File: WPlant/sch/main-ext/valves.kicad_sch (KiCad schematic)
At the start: 23 parts, among them J6 Conn_01x08_Pin, Q1 FDS9926A, Q2 FDS9926A, Q3 FDS9926A, Q4 FDS9926A, U7 74HC594

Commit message: Route of MainInt PCB done
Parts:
- J6: footprint easyeda2kicad:CONN-TH_8P-P2.50_XAD-8A -> locals:CONN-TH_8P-P2.50_XAD-8AS
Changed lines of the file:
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@@
 			)
 		)
-		(property "Footprint" "easyeda2kicad:CONN-TH_8P-P2.50_XAD-8A"
+		(property "Footprint" "locals:CONN-TH_8P-P2.50_XAD-8AS"
 			(at 212.09 93.98 0)
 			(effects

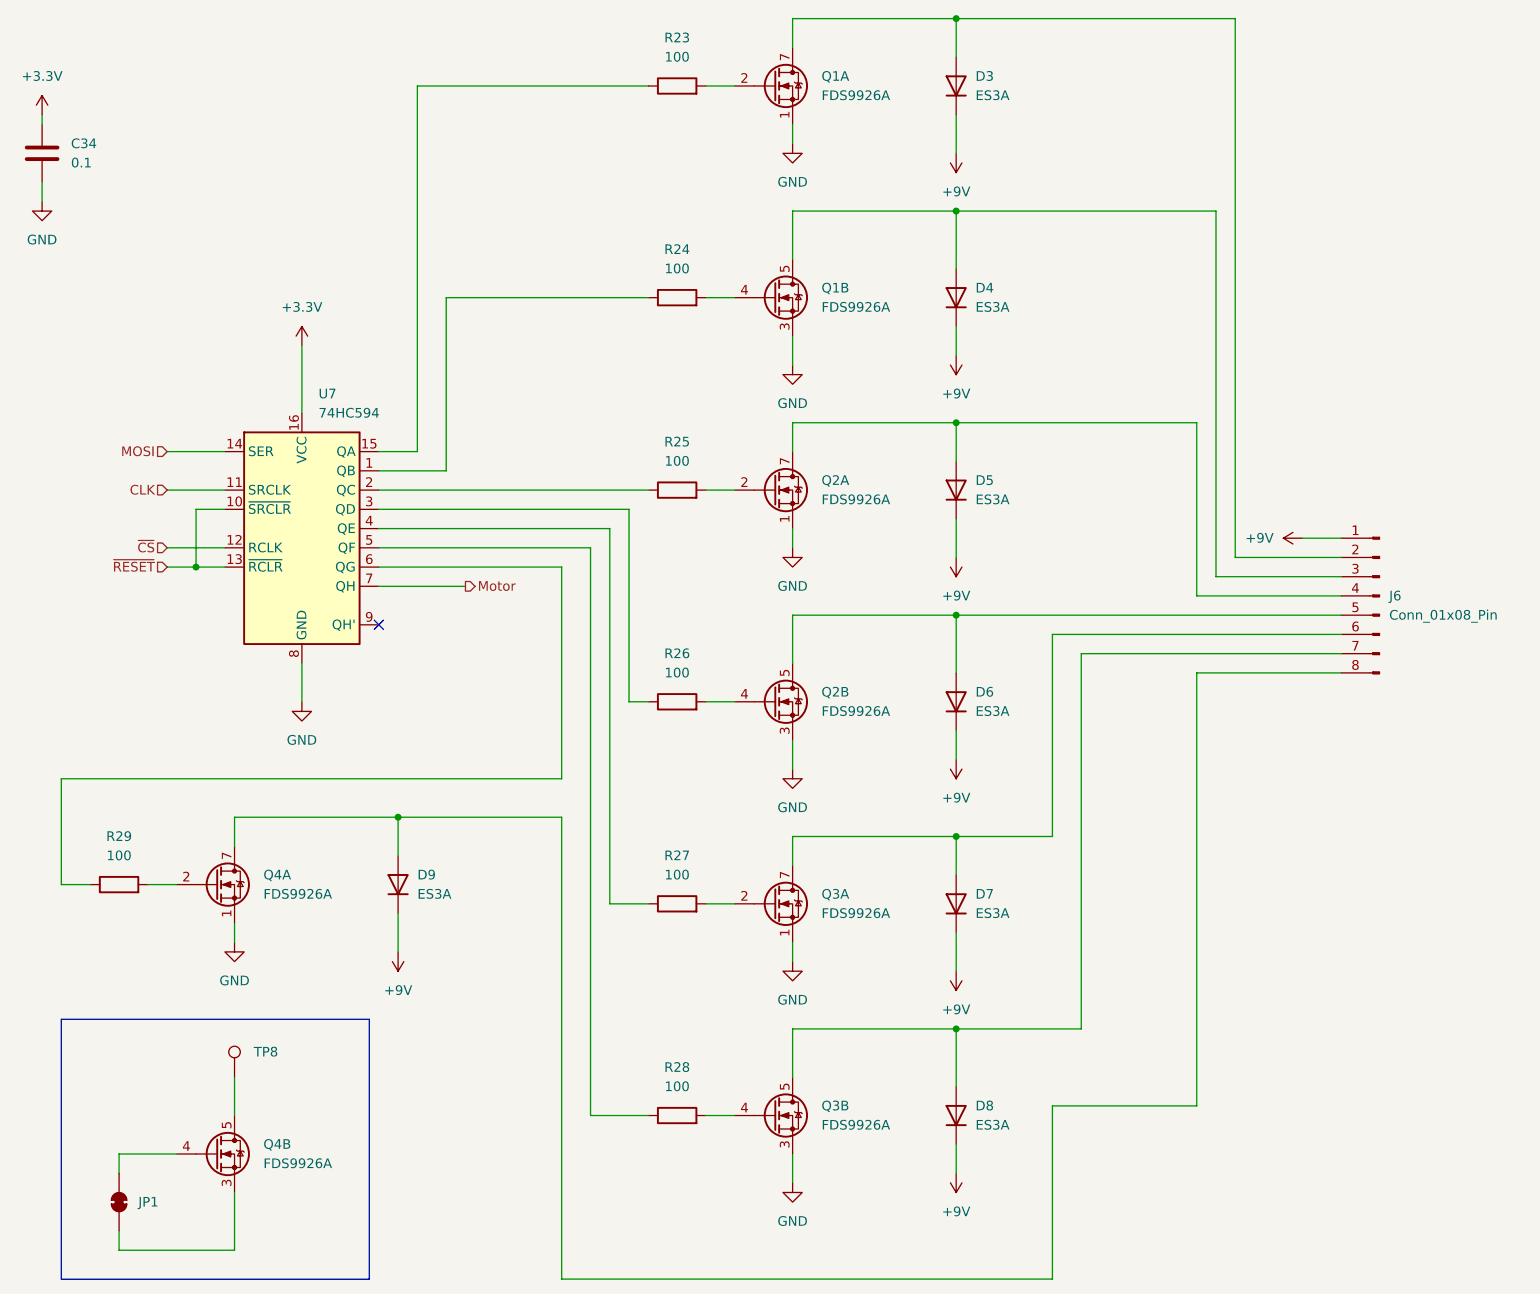
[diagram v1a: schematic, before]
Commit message: Route of MainExt PCB done
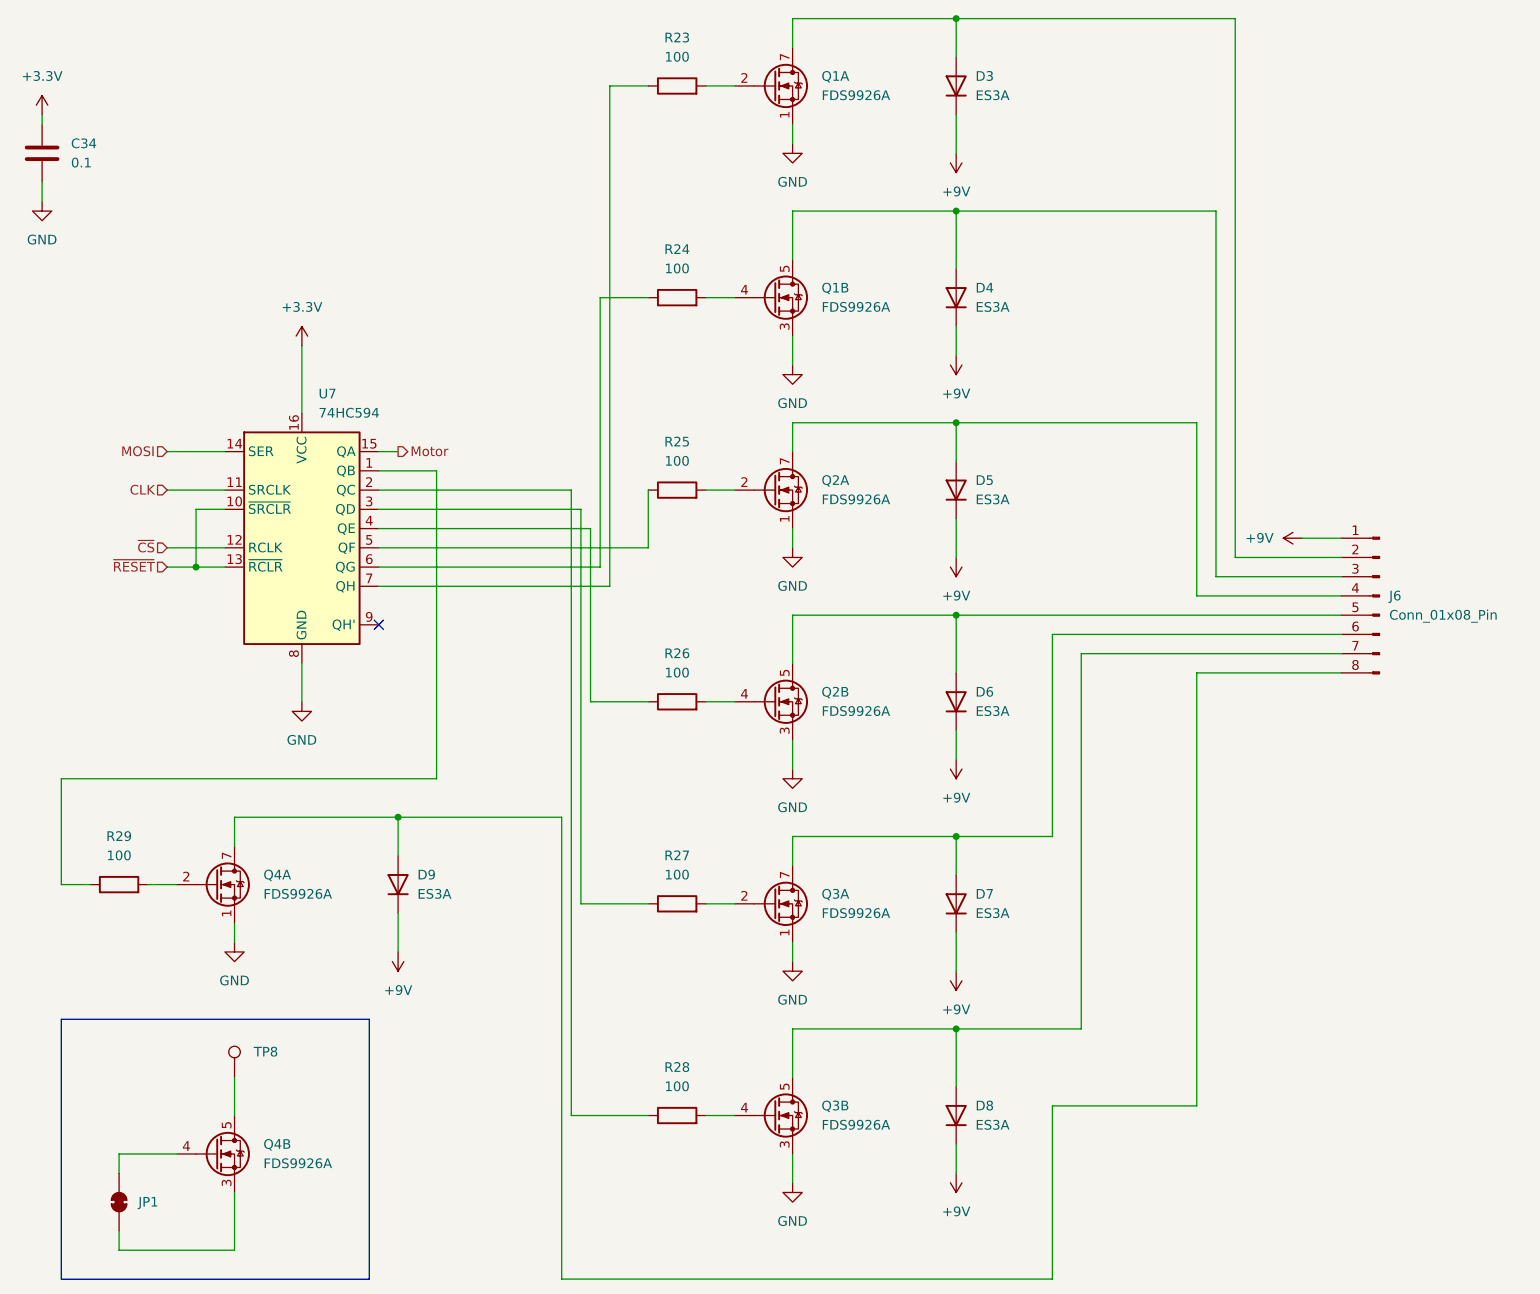
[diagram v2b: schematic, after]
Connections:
- net Motor: now also U7.15 (QA); no longer U7.7 (QH)
- net at R23.1: now also U7.7 (QH); no longer U7.15 (QA)
- net at R29.1: now also U7.1 (QB); no longer U7.6 (QG)
- net at R25.1: now also U7.5 (QF); no longer U7.2 (QC)
- net at R27.1: now also U7.3 (QD); no longer U7.4 (QE)
- net at R24.1: now also U7.6 (QG); no longer U7.1 (QB)
- net at R26.1: now also U7.4 (QE); no longer U7.3 (QD)
- net at R28.1: now also U7.2 (QC); no longer U7.5 (QF)
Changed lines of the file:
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@@
+	(wire
+		(pts
+			(xy 80.01 92.71) (xy 110.49 92.71)
+		)
+		(stroke
+			(width 0)
+			(type default)
+		)
+	)
 	(wire
 		(pts
@@
 	(wire
 		(pts
+			(xy 110.49 26.67) (xy 110.49 92.71)
+		)
+		(stroke
+			(width 0)
+			(type default)
+		)
+	)
+	(wire
+		(pts
+			(xy 106.68 82.55) (xy 106.68 134.62)
+		)
+		(stroke
+			(width 0)
+			(type default)
+		)
+	)
+	(wire
+		(pts
 			(xy 59.69 82.55) (xy 55.88 82.55)
 		)
@@
 	(wire
 		(pts
-			(xy 85.09 26.67) (xy 115.57 26.67)
-		)
-		(stroke
-			(width 0)
-			(type default)
-		)
-	)
-	(wire
-		(pts
 			(xy 156.21 96.52) (xy 207.01 96.52)
 		)
@@
 	(wire
 		(pts
-			(xy 80.01 80.01) (xy 115.57 80.01)
+			(xy 80.01 85.09) (xy 107.95 85.09)
 		)
 		(stroke
@@
 	(wire
 		(pts
-			(xy 113.03 82.55) (xy 113.03 107.95)
-		)
-		(stroke
-			(width 0)
-			(type default)
-		)
-	)
-	(wire
-		(pts
 			(xy 69.85 60.96) (xy 69.85 69.85)
 		)
@@
 	(wire
 		(pts
+			(xy 115.57 87.63) (xy 115.57 80.01)
+		)
+		(stroke
+			(width 0)
+			(type default)
+		)
+	)
+	(wire
+		(pts
+			(xy 105.41 80.01) (xy 105.41 162.56)
+		)
+		(stroke
+			(width 0)
+			(type default)
+		)
+	)
+	(wire
+		(pts
 			(xy 45.72 177.8) (xy 45.72 180.34)
 		)
@@
 	(wire
 		(pts
-			(xy 113.03 107.95) (xy 115.57 107.95)
+			(xy 107.95 107.95) (xy 115.57 107.95)
 		)
 		(stroke
@@
 	(wire
 		(pts
+			(xy 110.49 26.67) (xy 115.57 26.67)
+		)
+		(stroke
+			(width 0)
+			(type default)
+		)
+	)
+	(wire
+		(pts
 			(xy 60.96 162.56) (xy 60.96 157.48)
 		)
@@
 	(wire
 		(pts
-			(xy 104.14 118.11) (xy 38.1 118.11)
-		)
-		(stroke
-			(width 0)
-			(type default)
-		)
-	)
-	(wire
-		(pts
-			(xy 80.01 82.55) (xy 113.03 82.55)
+			(xy 87.63 118.11) (xy 38.1 118.11)
 		)
 		(stroke
@@
 	(wire
 		(pts
+			(xy 107.95 85.09) (xy 107.95 107.95)
+		)
+		(stroke
+			(width 0)
+			(type default)
+		)
+	)
+	(wire
+		(pts
 			(xy 134.62 125.73) (xy 156.21 125.73)
 		)
@@
 	(wire
 		(pts
+			(xy 87.63 77.47) (xy 80.01 77.47)
+		)
+		(stroke
+			(width 0)
+			(type default)
+		)
+	)
+	(wire
+		(pts
 			(xy 52.07 80.01) (xy 59.69 80.01)
 		)
@@
 	(wire
 		(pts
-			(xy 104.14 90.17) (xy 104.14 118.11)
-		)
-		(stroke
-			(width 0)
-			(type default)
-		)
-	)
-	(wire
-		(pts
 			(xy 52.07 87.63) (xy 59.69 87.63)
 		)
@@
 	(wire
 		(pts
-			(xy 80.01 92.71) (xy 91.44 92.71)
-		)
-		(stroke
-			(width 0)
-			(type default)
-		)
-	)
-	(wire
-		(pts
 			(xy 134.62 71.12) (xy 156.21 71.12)
 		)
@@
 	(wire
 		(pts
-			(xy 110.49 134.62) (xy 115.57 134.62)
+			(xy 80.01 87.63) (xy 115.57 87.63)
+		)
+		(stroke
+			(width 0)
+			(type default)
+		)
+	)
+	(wire
+		(pts
+			(xy 106.68 134.62) (xy 115.57 134.62)
 		)
 		(stroke
@@
 	(wire
 		(pts
-			(xy 80.01 85.09) (xy 110.49 85.09)
-		)
-		(stroke
-			(width 0)
-			(type default)
-		)
-	)
-	(wire
-		(pts
-			(xy 80.01 77.47) (xy 88.9 77.47)
-		)
-		(stroke
-			(width 0)
-			(type default)
-		)
-	)
-	(wire
-		(pts
 			(xy 172.72 101.6) (xy 207.01 101.6)
 		)
@@
 	(wire
 		(pts
-			(xy 88.9 77.47) (xy 88.9 54.61)
-		)
-		(stroke
-			(width 0)
-			(type default)
-		)
-	)
-	(wire
-		(pts
 			(xy 201.93 86.36) (xy 207.01 86.36)
 		)
@@
 	(wire
 		(pts
-			(xy 80.01 90.17) (xy 104.14 90.17)
-		)
-		(stroke
-			(width 0)
-			(type default)
-		)
-	)
-	(wire
-		(pts
 			(xy 123.19 80.01) (xy 127 80.01)
 		)
@@
 	(wire
 		(pts
-			(xy 85.09 74.93) (xy 85.09 26.67)
-		)
-		(stroke
-			(width 0)
-			(type default)
-		)
-	)
-	(wire
-		(pts
 			(xy 156.21 111.76) (xy 156.21 115.57)
 		)
@@
 	(wire
 		(pts
-			(xy 107.95 162.56) (xy 115.57 162.56)
+			(xy 105.41 162.56) (xy 115.57 162.56)
 		)
 		(stroke
@@
 	(wire
 		(pts
-			(xy 80.01 87.63) (xy 107.95 87.63)
-		)
-		(stroke
-			(width 0)
-			(type default)
-		)
-	)
-	(wire
-		(pts
 			(xy 123.19 54.61) (xy 127 54.61)
 		)
@@
 	(wire
 		(pts
-			(xy 110.49 85.09) (xy 110.49 134.62)
+			(xy 80.01 90.17) (xy 109.22 90.17)
 		)
 		(stroke
@@
 	(wire
 		(pts
+			(xy 109.22 54.61) (xy 115.57 54.61)
+		)
+		(stroke
+			(width 0)
+			(type default)
+		)
+	)
+	(wire
+		(pts
 			(xy 207.01 88.9) (xy 193.04 88.9)
 		)
@@
 	(wire
 		(pts
+			(xy 109.22 54.61) (xy 109.22 90.17)
+		)
+		(stroke
+			(width 0)
+			(type default)
+		)
+	)
+	(wire
+		(pts
 			(xy 134.62 17.78) (xy 156.21 17.78)
 		)
@@
 	(wire
 		(pts
-			(xy 88.9 54.61) (xy 115.57 54.61)
+			(xy 82.55 74.93) (xy 80.01 74.93)
 		)
 		(stroke
@@
 	(wire
 		(pts
-			(xy 107.95 87.63) (xy 107.95 162.56)
+			(xy 87.63 77.47) (xy 87.63 118.11)
 		)
 		(stroke
@@
 	(wire
 		(pts
-			(xy 80.01 74.93) (xy 85.09 74.93)
-		)
-		(stroke
-			(width 0)
-			(type default)
-		)
-	)
-	(wire
-		(pts
 			(xy 187.96 93.98) (xy 207.01 93.98)
 		)
@@
 	(wire
 		(pts
+			(xy 80.01 80.01) (xy 105.41 80.01)
+		)
+		(stroke
+			(width 0)
+			(type default)
+		)
+	)
+	(wire
+		(pts
 			(xy 45.72 167.64) (xy 53.34 167.64)
+		)
+		(stroke
+			(width 0)
+			(type default)
+		)
+	)
+	(wire
+		(pts
+			(xy 80.01 82.55) (xy 106.68 82.55)
 		)
 		(stroke
@@
 	(hierarchical_label "Motor"
 		(shape output)
-		(at 91.44 92.71 0)
+		(at 82.55 74.93 0)
 		(fields_autoplaced yes)
 		(effects

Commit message: Update WP Sch (sheets titles, replaced wires by bus, update components values)
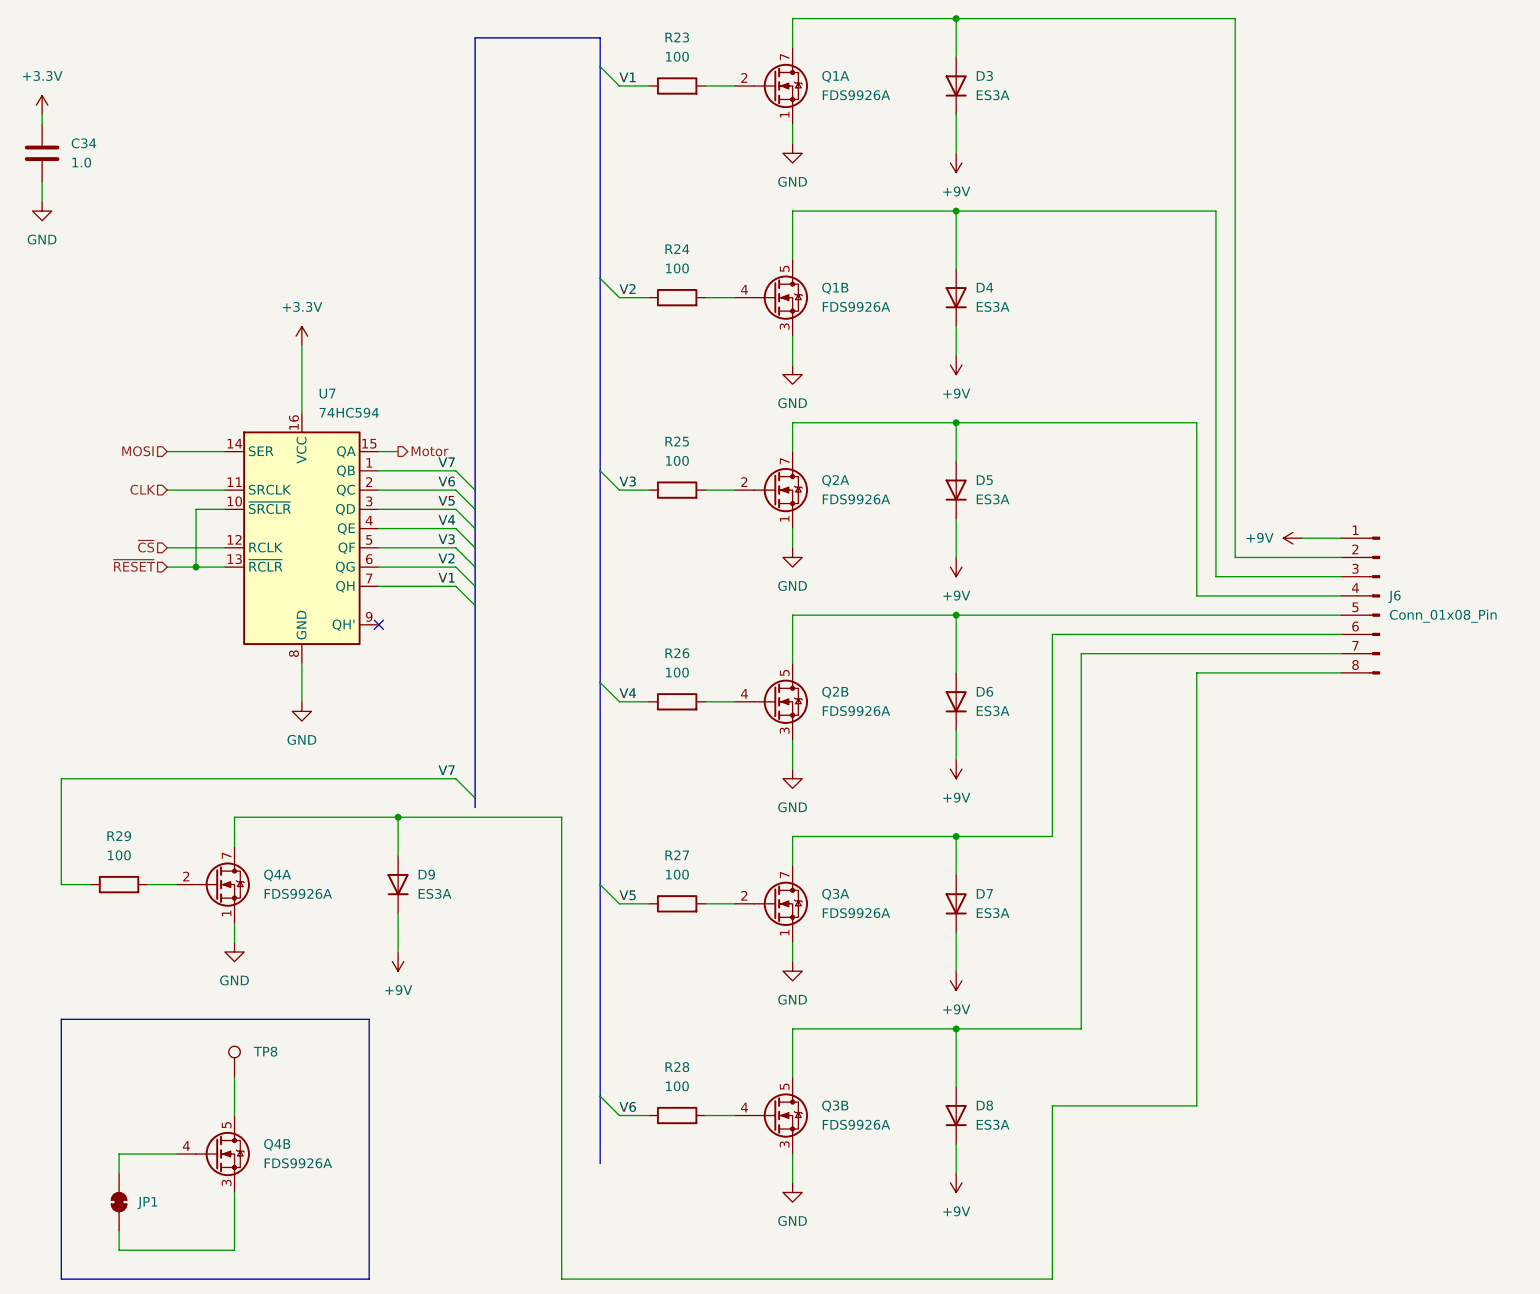
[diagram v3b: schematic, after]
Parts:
- C34: value 0.1 -> 1.0
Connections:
- net V1: now reaches R23.1, U7.7 (QH)
- net V7: now reaches R29.1, U7.1 (QB)
- net V3: now reaches R25.1, U7.5 (QF)
- net V5: now reaches R27.1, U7.3 (QD)
- net V6: now reaches R28.1, U7.2 (QC)
- net V4: now reaches R26.1, U7.4 (QE)
- net V2: now reaches R24.1, U7.6 (QG)
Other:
- title: Valves interface -> Valves interface  (WPMain Ext)
